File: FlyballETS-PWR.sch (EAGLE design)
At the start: 8 parts

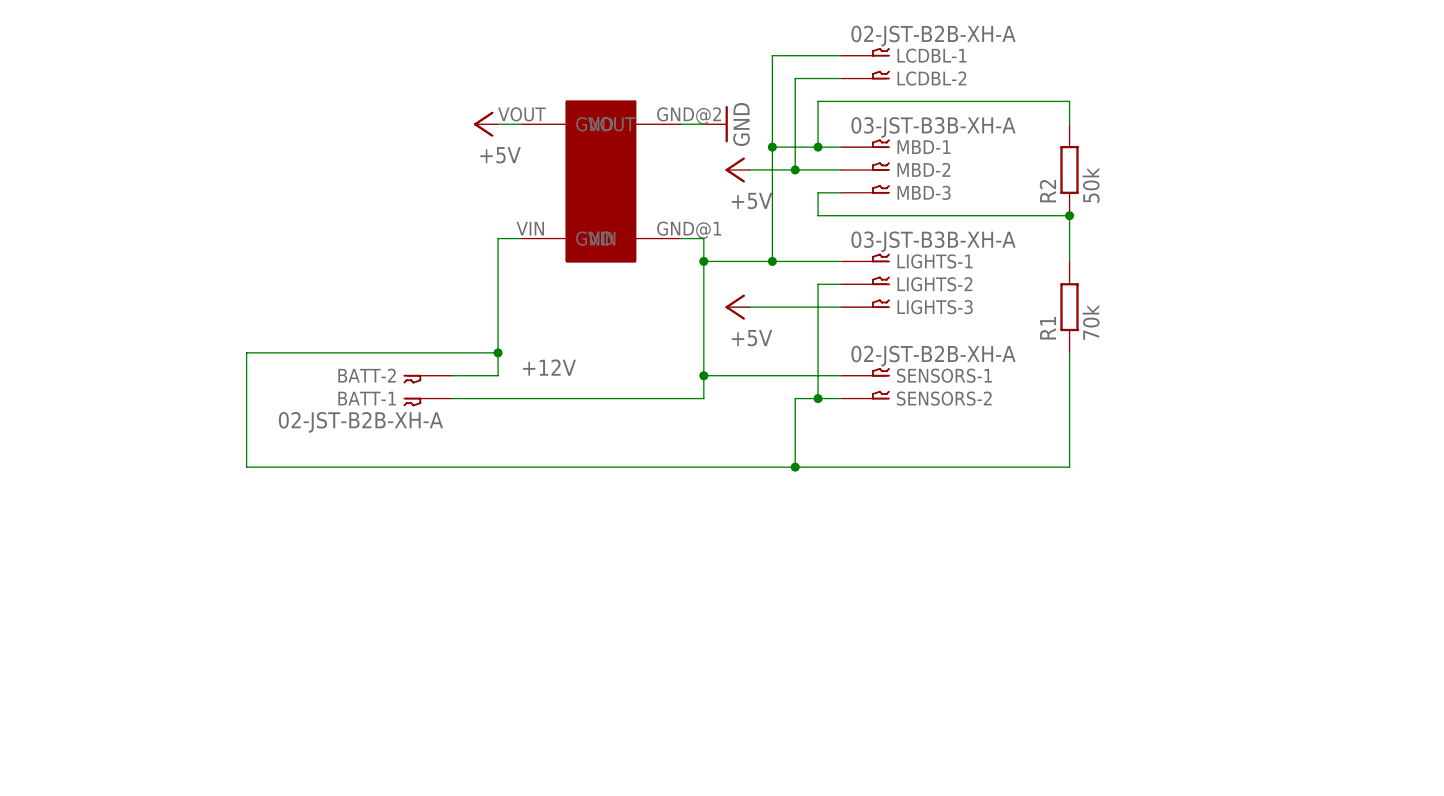
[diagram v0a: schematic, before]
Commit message: Updated drawings and added PNG exports
- Added frames around drawings to make it look neater
- Added PNG export files so people who don't have EAGLE can see
everything
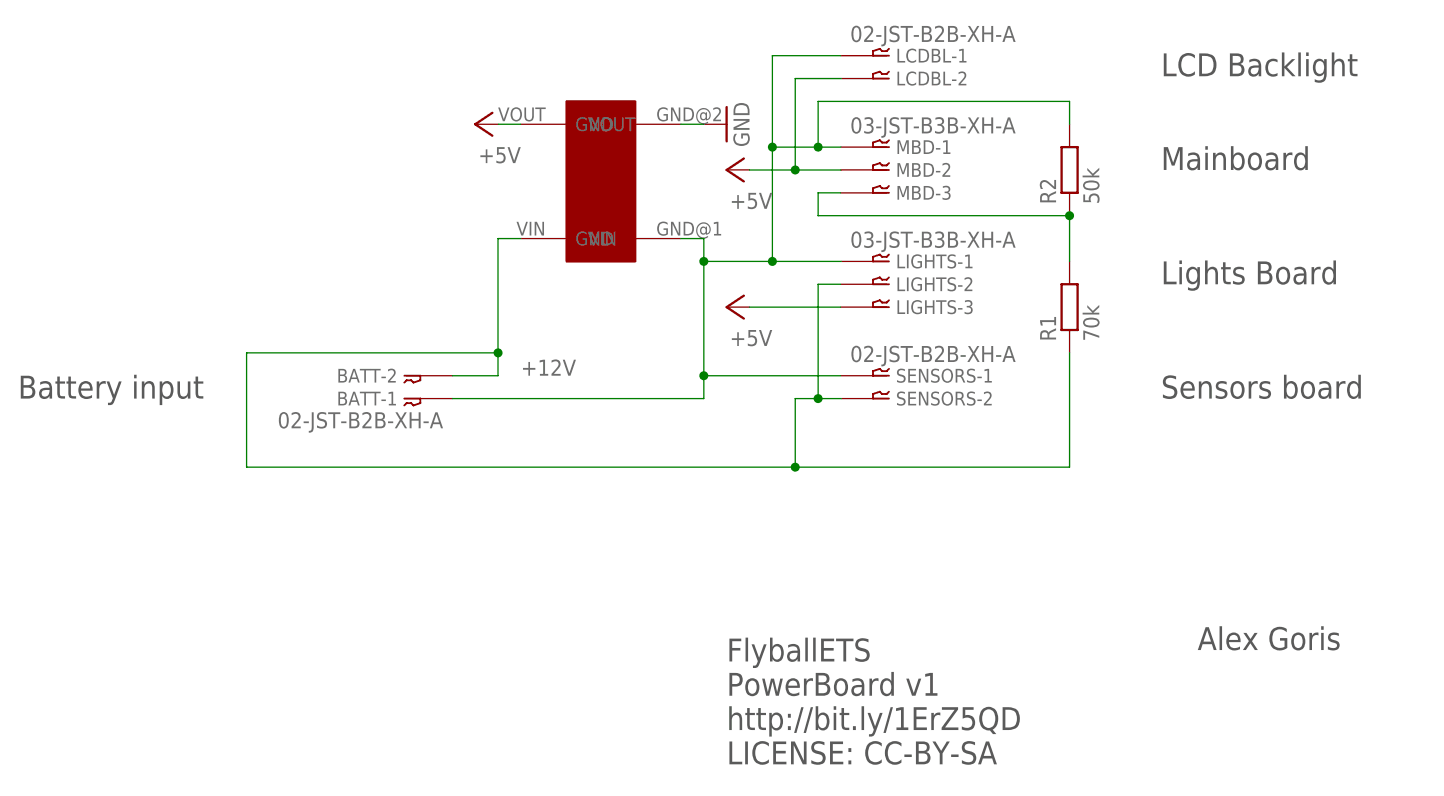
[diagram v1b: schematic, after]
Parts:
- renumbered U$3 to U$1
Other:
- note added: "Alex Goris"
- note added: "Battery input"
- note added: "FlyballETS PowerBoard v1 http://bit.ly/1ErZ5QD LICENSE: CC-BY-SA"
- note added: "LCD Backlight"
- note added: "Lights Board"
- note added: "Mainboard"
- note added: "Sensors board"
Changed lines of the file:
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@@
 <part name="MBD" library="bt_con-jst-xh" deviceset="03-JST" device="-B3B-XH-A"/>
 <part name="R1" library="resistor" deviceset="R-EU_" device="0204/5" value="70k"/>
-<part name="U$3" library="_custom" deviceset="LM2596-BOARD" device=""/>
 <part name="P+1" library="supply1" deviceset="+5V" device=""/>
 <part name="GND3" library="supply1" deviceset="GND" device=""/>
@@
 <part name="R2" library="resistor" deviceset="R-EU_" device="0204/5" value="50k"/>
 <part name="LCDBL" library="bt_con-jst-xh" deviceset="02-JST" device="-B2B-XH-A"/>
+<part name="U$1" library="_custom" deviceset="LM2596-BOARD" device=""/>
+<part name="FRAME1" library="frames" deviceset="A5L-LOC" device=""/>
 </parts>
 <sheets>
 <sheet>
 <plain>
+<text x="50.8" y="-35.56" size="2.54" layer="97">FlyballETS
+PowerBoard v1
+http://bit.ly/1ErZ5QD
+LICENSE: CC-BY-SA</text>
+<text x="103.124" y="-22.86" size="2.54" layer="97">Alex Goris</text>
+<text x="99.06" y="30.48" size="2.54" layer="97">Mainboard</text>
+<text x="99.06" y="40.894" size="2.54" layer="97">LCD Backlight</text>
+<text x="99.06" y="17.78" size="2.54" layer="97">Lights Board</text>
+<text x="99.06" y="5.08" size="2.54" layer="97">Sensors board</text>
+<text x="-27.94" y="5.08" size="2.54" layer="97">Battery input</text>
 </plain>
 <instances>
@@
 <instance part="MBD" gate="-3" x="68.58" y="27.94"/>
 <instance part="R1" gate="G$1" x="88.9" y="15.24" rot="R90"/>
-<instance part="U$3" gate="G$1" x="33.02" y="22.86"/>
 <instance part="P+1" gate="1" x="22.86" y="35.56" rot="R90"/>
 <instance part="GND3" gate="1" x="50.8" y="35.56" rot="R90"/>
@@
 <instance part="LCDBL" gate="-1" x="68.58" y="43.18"/>
 <instance part="LCDBL" gate="-2" x="68.58" y="40.64"/>
+<instance part="U$1" gate="G$1" x="33.02" y="22.86"/>
+<instance part="FRAME1" gate="G$1" x="-38.1" y="-43.18"/>
 </instances>
 <busses>
@@
 <net name="+5V" class="0">
 <segment>
-<pinref part="U$3" gate="G$1" pin="VOUT"/>
 <pinref part="P+1" gate="1" pin="+5V"/>
 <wire x1="27.94" y1="35.56" x2="25.4" y2="35.56" width="0.1524" layer="91"/>
+<pinref part="U$1" gate="G$1" pin="VOUT"/>
 </segment>
 <segment>
@@
 <wire x1="20.32" y1="5.08" x2="48.26" y2="5.08" width="0.1524" layer="91"/>
 <wire x1="48.26" y1="5.08" x2="48.26" y2="7.62" width="0.1524" layer="91"/>
-<pinref part="U$3" gate="G$1" pin="GND@1"/>
 <wire x1="48.26" y1="7.62" x2="48.26" y2="20.32" width="0.1524" layer="91"/>
 <wire x1="48.26" y1="20.32" x2="48.26" y2="22.86" width="0.1524" layer="91"/>
@@
 <pinref part="LCDBL" gate="-1" pin="1"/>
 <wire x1="55.88" y1="43.18" x2="63.5" y2="43.18" width="0.1524" layer="91"/>
+<pinref part="U$1" gate="G$1" pin="GND@1"/>
 </segment>
 <segment>
-<pinref part="U$3" gate="G$1" pin="GND@2"/>
 <pinref part="GND3" gate="1" pin="GND"/>
 <wire x1="45.72" y1="35.56" x2="48.26" y2="35.56" width="0.1524" layer="91"/>
+<pinref part="U$1" gate="G$1" pin="GND@2"/>
 </segment>
 </net>
@@
 <wire x1="20.32" y1="7.62" x2="25.4" y2="7.62" width="0.1524" layer="91"/>
 <wire x1="25.4" y1="7.62" x2="25.4" y2="10.16" width="0.1524" layer="91"/>
-<pinref part="U$3" gate="G$1" pin="VIN"/>
 <wire x1="25.4" y1="10.16" x2="25.4" y2="22.86" width="0.1524" layer="91"/>
 <wire x1="25.4" y1="22.86" x2="27.94" y2="22.86" width="0.1524" layer="91"/>
@@
 <wire x1="88.9" y1="-2.54" x2="88.9" y2="10.16" width="0.1524" layer="91"/>
 <pinref part="R1" gate="G$1" pin="1"/>
+<pinref part="U$1" gate="G$1" pin="VIN"/>
 </segment>
 </net>
@@
 </schematic>
 </drawing>
+<compatibility>
+<note version="6.3" minversion="6.2.2" severity="warning">
+Since Version 6.2.2 text objects can contain more than one line,
+which will not be processed correctly with this version.
+</note>
+</compatibility>
 </eagle>

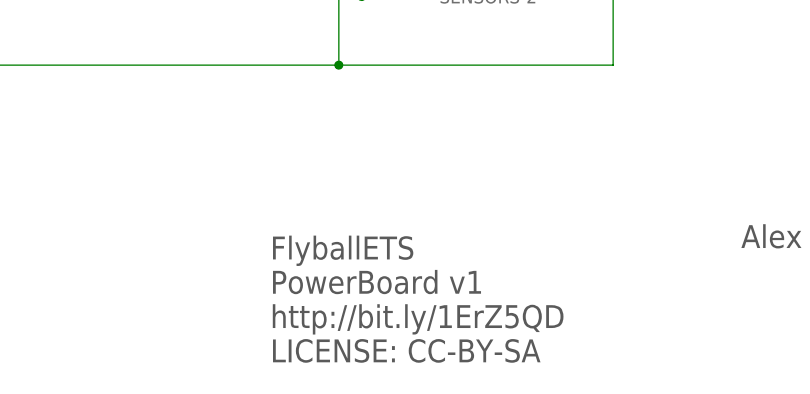
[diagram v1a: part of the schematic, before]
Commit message: v2 release of remaining boards.
- Lightsboard: Corrected swapped pin connections on L2 side and made
smaller
- Powerboard: Made smaller and added descriptions for LM2596 board
- Sensorboard: Made smaller
- All boards: Removed JST connector type names
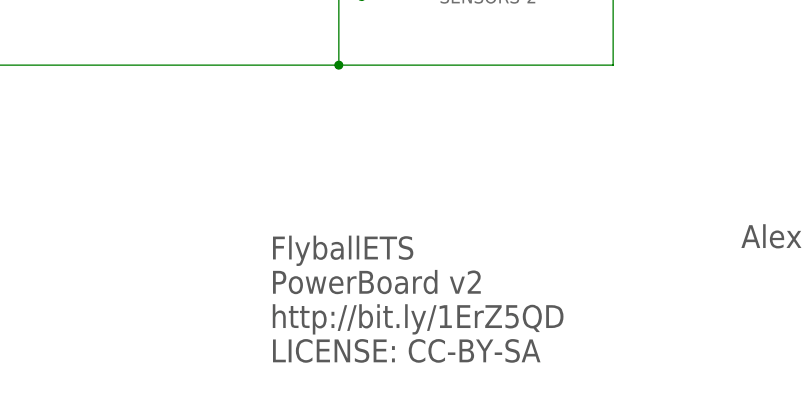
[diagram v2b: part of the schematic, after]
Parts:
- R1, R2: device resistor:R-EU_0204/5 -> resistor:R-EU_0207/10
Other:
- note added: "FlyballETS PowerBoard v2 http://bit.ly/1ErZ5QD LICENSE: CC-BY-SA"
- note removed: "FlyballETS PowerBoard v1 http://bit.ly/1ErZ5QD LICENSE: CC-BY-SA"
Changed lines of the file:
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@@
 <?xml version="1.0" encoding="utf-8"?>
 <!DOCTYPE eagle SYSTEM "eagle.dtd">
-<eagle version="7.3.0">
+<eagle version="7.5.0">
 <drawing>
 <settings>
@@
 <setting verticaltext="up"/>
 </settings>
-<grid distance="2.54" unitdist="mm" unit="mm" style="lines" multiple="1" display="yes" altdistance="0.01" altunitdist="inch" altunit="inch"/>
+<grid distance="0.1" unitdist="inch" unit="inch" style="lines" multiple="1" display="no" altdistance="0.01" altunitdist="inch" altunit="inch"/>
 <layers>
 <layer number="1" name="Top" color="4" fill="1" visible="no" active="no"/>
@@
 <part name="BATT" library="bt_con-jst-xh" deviceset="02-JST" device="-B2B-XH-A"/>
 <part name="MBD" library="bt_con-jst-xh" deviceset="03-JST" device="-B3B-XH-A"/>
-<part name="R1" library="resistor" deviceset="R-EU_" device="0204/5" value="70k"/>
+<part name="R1" library="resistor" deviceset="R-EU_" device="0207/10" value="70k"/>
 <part name="P+1" library="supply1" deviceset="+5V" device=""/>
 <part name="GND3" library="supply1" deviceset="GND" device=""/>
@@
 <part name="P+3" library="supply1" deviceset="+5V" device=""/>
 <part name="P+5" library="supply1" deviceset="+5V" device=""/>
-<part name="R2" library="resistor" deviceset="R-EU_" device="0204/5" value="50k"/>
+<part name="R2" library="resistor" deviceset="R-EU_" device="0207/10" value="50k"/>
 <part name="LCDBL" library="bt_con-jst-xh" deviceset="02-JST" device="-B2B-XH-A"/>
 <part name="U$1" library="_custom" deviceset="LM2596-BOARD" device=""/>
@@
 <plain>
 <text x="50.8" y="-35.56" size="2.54" layer="97">FlyballETS
-PowerBoard v1
+PowerBoard v2
 http://bit.ly/1ErZ5QD
 LICENSE: CC-BY-SA</text>

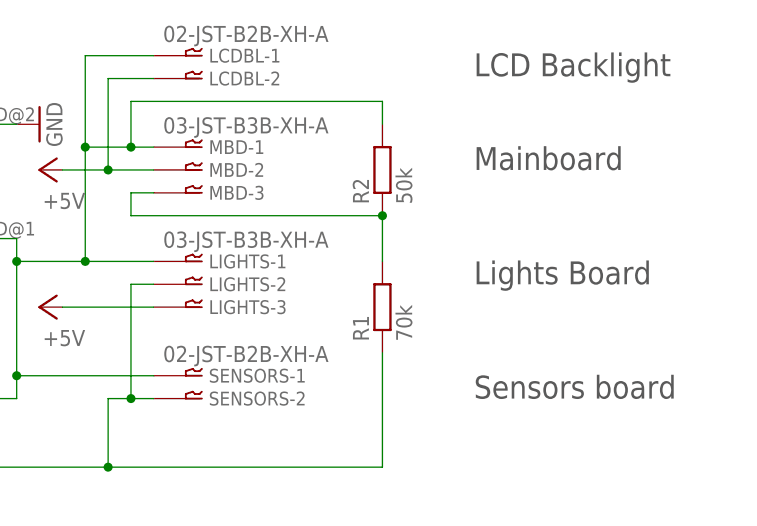
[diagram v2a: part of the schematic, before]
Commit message: Changed resistor values to more practical ones
Changed R1 to 5.6kOhm, R2 to 3.9kOhm. These are common values in
resistor assortments. Fixes #2
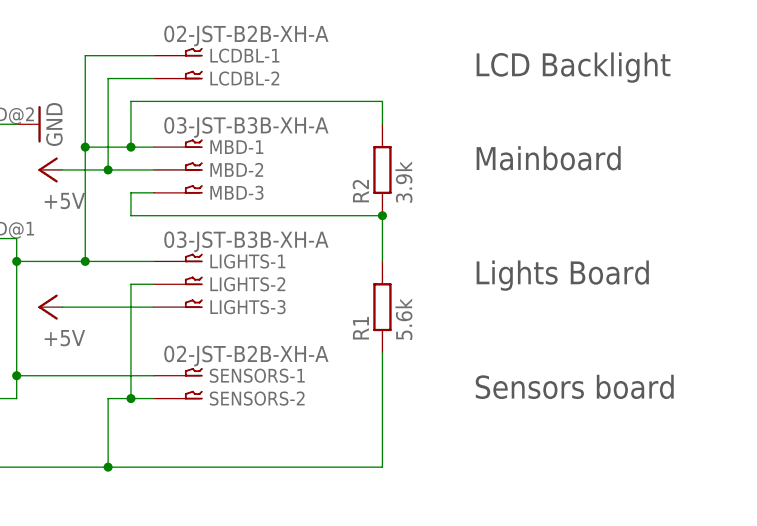
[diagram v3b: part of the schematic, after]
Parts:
- R1: value 70k -> 5.6k
- R2: value 50k -> 3.9k
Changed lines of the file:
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@@
 <part name="BATT" library="bt_con-jst-xh" deviceset="02-JST" device="-B2B-XH-A"/>
 <part name="MBD" library="bt_con-jst-xh" deviceset="03-JST" device="-B3B-XH-A"/>
-<part name="R1" library="resistor" deviceset="R-EU_" device="0207/10" value="70k"/>
+<part name="R1" library="resistor" deviceset="R-EU_" device="0207/10" value="5.6k"/>
 <part name="P+1" library="supply1" deviceset="+5V" device=""/>
 <part name="GND3" library="supply1" deviceset="GND" device=""/>
@@
 <part name="P+3" library="supply1" deviceset="+5V" device=""/>
 <part name="P+5" library="supply1" deviceset="+5V" device=""/>
-<part name="R2" library="resistor" deviceset="R-EU_" device="0207/10" value="50k"/>
+<part name="R2" library="resistor" deviceset="R-EU_" device="0207/10" value="3.9k"/>
 <part name="LCDBL" library="bt_con-jst-xh" deviceset="02-JST" device="-B2B-XH-A"/>
 <part name="U$1" library="_custom" deviceset="LM2596-BOARD" device=""/>

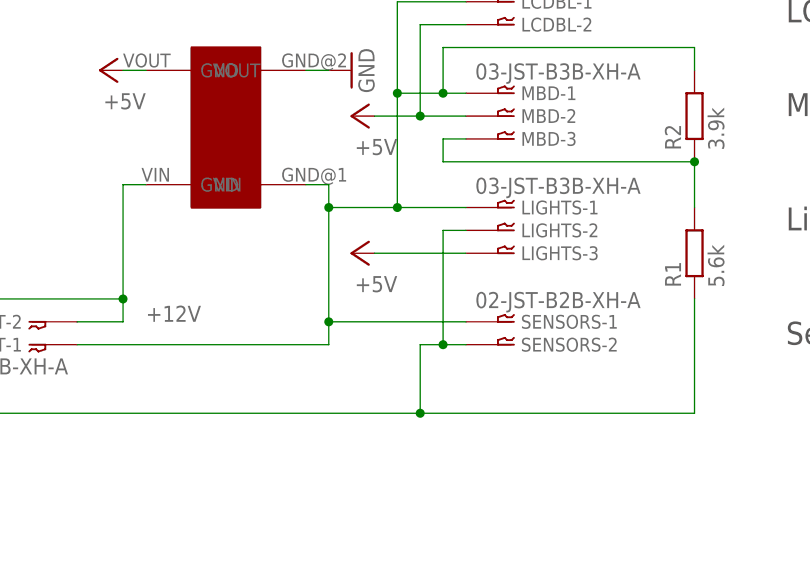
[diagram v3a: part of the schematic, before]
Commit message: Fixed several issues
- Checked all mounting holes (fixes #1 )
- Marked light colors on lights PCB (fixes #7 )
- Swapped pins 2 and 3 on LIGHTS connected on PWR board (fixes #3 )
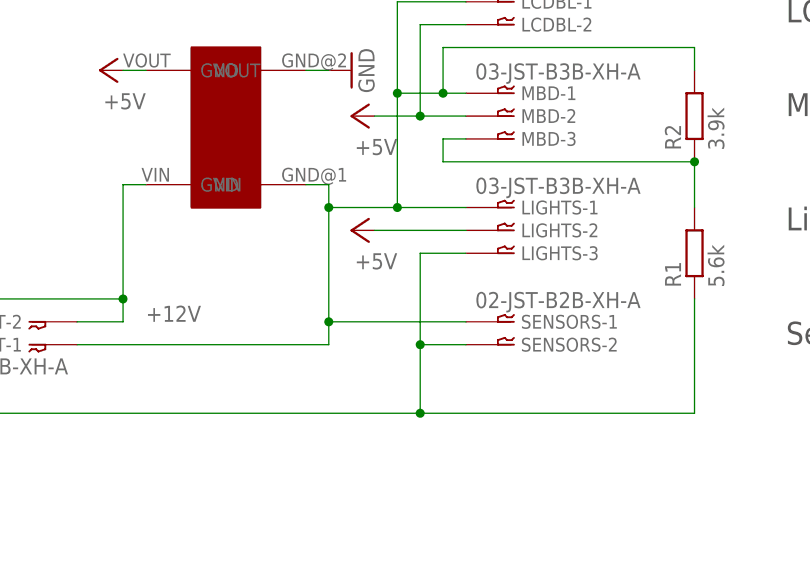
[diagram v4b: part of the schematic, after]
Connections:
- net +12V: now also LIGHTS-3.1; no longer LIGHTS-2.1
- net +5V: now also LIGHTS-2.1; no longer LIGHTS-3.1
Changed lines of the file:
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@@
 <instance part="LIGHTS" gate="-2" x="68.58" y="17.78"/>
 <instance part="LIGHTS" gate="-3" x="68.58" y="15.24"/>
-<instance part="P+3" gate="1" x="50.8" y="15.24" rot="R90"/>
+<instance part="P+3" gate="1" x="50.8" y="17.78" rot="R90"/>
 <instance part="P+5" gate="1" x="50.8" y="30.48" rot="R90"/>
 <instance part="R2" gate="G$1" x="88.9" y="30.48" rot="R90"/>
@@
 </segment>
 <segment>
-<pinref part="P+3" gate="1" pin="+5V"/>
-<pinref part="LIGHTS" gate="-3" pin="1"/>
-<wire x1="53.34" y1="15.24" x2="63.5" y2="15.24" width="0.1524" layer="91"/>
-</segment>
-<segment>
 <pinref part="P+5" gate="1" pin="+5V"/>
 <pinref part="MBD" gate="-2" pin="1"/>
@@
 <pinref part="LCDBL" gate="-2" pin="1"/>
 <wire x1="58.42" y1="40.64" x2="63.5" y2="40.64" width="0.1524" layer="91"/>
+</segment>
+<segment>
+<pinref part="P+3" gate="1" pin="+5V"/>
+<pinref part="LIGHTS" gate="-2" pin="1"/>
+<wire x1="53.34" y1="17.78" x2="63.5" y2="17.78" width="0.1524" layer="91"/>
 </segment>
 </net>
@@
 <wire x1="58.42" y1="-2.54" x2="58.42" y2="5.08" width="0.1524" layer="91"/>
 <pinref part="SENSORS" gate="-2" pin="1"/>
-<wire x1="58.42" y1="5.08" x2="60.96" y2="5.08" width="0.1524" layer="91"/>
-<wire x1="60.96" y1="5.08" x2="63.5" y2="5.08" width="0.1524" layer="91"/>
-<wire x1="60.96" y1="5.08" x2="60.96" y2="17.78" width="0.1524" layer="91"/>
-<junction x="60.96" y="5.08"/>
-<pinref part="LIGHTS" gate="-2" pin="1"/>
-<wire x1="60.96" y1="17.78" x2="63.5" y2="17.78" width="0.1524" layer="91"/>
+<wire x1="58.42" y1="5.08" x2="63.5" y2="5.08" width="0.1524" layer="91"/>
 <wire x1="58.42" y1="-2.54" x2="88.9" y2="-2.54" width="0.1524" layer="91"/>
 <junction x="58.42" y="-2.54"/>
@@
 <pinref part="R1" gate="G$1" pin="1"/>
 <pinref part="U$1" gate="G$1" pin="VIN"/>
+<pinref part="LIGHTS" gate="-3" pin="1"/>
+<wire x1="63.5" y1="15.24" x2="58.42" y2="15.24" width="0.1524" layer="91"/>
+<wire x1="58.42" y1="15.24" x2="58.42" y2="5.08" width="0.1524" layer="91"/>
+<junction x="58.42" y="5.08"/>
 </segment>
 </net>
